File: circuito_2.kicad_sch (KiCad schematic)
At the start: 25 parts, among them U1 TL081, U2 TL081, U3 TL081

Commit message: Reorganização dos esquemáticos em pages.
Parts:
- removed C1, C10, C11, C13, C15, C2, C4, C7, C8: C, symbol Device:C
- removed C12, C14, C3, C5, C6, C9: C_Polarized_US, symbol Device:C_Polarized_US
- removed R1, R2, R3, R4, R5, R6, R7: R, symbol Device:R
- removed U1, U2, U3: TL081, symbol Amplifier_Operational:TL081
- added C22, C24, C25, C28, C29, C31, C33, C34, C36: C, symbol Device:C
- added C23, C26, C27, C30, C32, C35: C_Polarized_US, symbol Device:C_Polarized_US
- added R10, R11, R12, R13, R14, R8, R9: R, symbol Device:R
- added U10, U8, U9: TL081, symbol Amplifier_Operational:TL081
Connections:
- net +15V: now also C23.1, C24.1, C27.1, C28.1, C32.1, C33.1, U10.7 (V+), U8.7 (V+), U9.7 (V+)
- net -15V: now also C25.1, C26.2, C29.1, C30.2, C34.1, C35.2, U10.4 (V-), U8.4 (V-), U9.4 (V-)
- net Earth: now also C22.2, C23.2, C24.2, C25.2, C26.1, C27.2, C28.2, C29.2, C30.1, C32.2, C33.2, C34.2, C35.1, R8.2, U9.3 (+)
- new net: C22.1, R10.1, U8.2 (-)
- new net: C36.1, R13.2, R14.1, U10.2 (-)
- new net: C36.2, R14.2, U10.6
- new net: C31.2, R12.2, R13.1, U9.6
- new net: R8.1, R9.1, U8.3 (+)
- new net: R10.2, R11.1, R9.2, U8.6
- new net: C31.1, R11.2, R12.1, U9.2 (-)

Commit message: Footprints parcialmente adicionados.
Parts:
- C10: renamed from C25; value C -> 0.1uF/50V; footprint (none) -> Capacitor_THT:C_Disc_D3.8mm_W2.6mm_P2.50mm
- C13: renamed from C28; value C -> 0.1uF/50V; footprint (none) -> Capacitor_THT:C_Disc_D3.8mm_W2.6mm_P2.50mm
- C14: renamed from C29; value C -> 0.1uF/50V; footprint (none) -> Capacitor_THT:C_Disc_D3.8mm_W2.6mm_P2.50mm
- C16: renamed from C31; value C -> 0.1uF/50V; footprint (none) -> Capacitor_THT:C_Disc_D3.8mm_W2.6mm_P2.50mm
- C18: renamed from C33; value C -> 0.1uF/50V; footprint (none) -> Capacitor_THT:C_Disc_D3.8mm_W2.6mm_P2.50mm
- C19: renamed from C34; value C -> 0.1uF/50V; footprint (none) -> Capacitor_THT:C_Disc_D3.8mm_W2.6mm_P2.50mm
- C21: renamed from C36; value C -> 0.1uF/50V; footprint (none) -> Capacitor_THT:C_Disc_D3.8mm_W2.6mm_P2.50mm
- C7: renamed from C22; value C -> 0.1uF/50V; footprint (none) -> Capacitor_THT:C_Disc_D3.8mm_W2.6mm_P2.50mm
- C9: renamed from C24; value C -> 0.1uF/50V; footprint (none) -> Capacitor_THT:C_Disc_D3.8mm_W2.6mm_P2.50mm
- renumbered C26 to C11, C27 to C12, C30 to C15, C32 to C17, C35 to C20, C23 to C8, R8 to R1, R9 to R2, R10 to R3, R11 to R4, R12 to R5, R13 to R6, R14 to R7, U8 to U3, U9 to U4, U10 to U5
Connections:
- net Senoidal: now reaches C21.2, R7.2, U5.6
- net Triangular: now reaches C16.2, R5.2, R6.1, U4.6
- net Quadrada: now reaches R2.2, R3.2, R4.1, U3.6

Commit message: Relação de footprints finalizada.
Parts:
- C11, C12, C15, C17, C20, C8: value C_Polarized_US -> 10uF/25V; footprint (none) -> Capacitor_THT:CP_Radial_D4.0mm_P2.00mm
- R1, R2, R3, R4, R5, R6, R7: footprint (none) -> Resistor_THT:R_Axial_DIN0207_L6.3mm_D2.5mm_P2.54mm_Vertical
- U3, U4, U5: footprint (none) -> Package_DIP:DIP-8_W7.62mm_LongPads
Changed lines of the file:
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@@
 			)
 		)
-		(property "Value" "C_Polarized_US"
+		(property "Value" "10uF/25V"
 			(at 75.565 106.68 90)
 			(effects
@@
 			)
 		)
-		(property "Footprint" ""
+		(property "Footprint" "Capacitor_THT:CP_Radial_D4.0mm_P2.00mm"
 			(at 74.93 111.76 0)
 			(effects
@@
 			)
 		)
-		(property "Value" "C_Polarized_US"
+		(property "Value" "10uF/25V"
 			(at 132.715 58.42 90)
 			(effects
@@
 			)
 		)
-		(property "Footprint" ""
+		(property "Footprint" "Capacitor_THT:CP_Radial_D4.0mm_P2.00mm"
 			(at 133.35 63.5 0)
 			(effects
@@
 			)
 		)
-		(property "Footprint" ""
+		(property "Footprint" "Resistor_THT:R_Axial_DIN0207_L6.3mm_D2.5mm_P2.54mm_Vertical"
 			(at 196.85 137.668 90)
 			(effects
@@
 			)
 		)
-		(property "Value" "C_Polarized_US"
+		(property "Value" "10uF/25V"
 			(at 74.295 59.69 90)
 			(effects
@@
 			)
 		)
-		(property "Footprint" ""
+		(property "Footprint" "Capacitor_THT:CP_Radial_D4.0mm_P2.00mm"
 			(at 74.93 64.77 0)
 			(effects
@@
 			)
 		)
-		(property "Footprint" ""
+		(property "Footprint" "Resistor_THT:R_Axial_DIN0207_L6.3mm_D2.5mm_P2.54mm_Vertical"
 			(at 163.83 85.598 90)
 			(effects
@@
 			)
 		)
-		(property "Footprint" ""
+		(property "Footprint" "Package_DIP:DIP-8_W7.62mm_LongPads"
 			(at 74.93 85.09 0)
 			(effects
@@
 			)
 		)
-		(property "Footprint" ""
+		(property "Footprint" "Resistor_THT:R_Axial_DIN0207_L6.3mm_D2.5mm_P2.54mm_Vertical"
 			(at 83.82 124.968 90)
 			(effects
@@
 			)
 		)
-		(property "Footprint" ""
+		(property "Footprint" "Resistor_THT:R_Axial_DIN0207_L6.3mm_D2.5mm_P2.54mm_Vertical"
 			(at 106.68 88.138 90)
 			(effects
@@
 			)
 		)
-		(property "Footprint" ""
+		(property "Footprint" "Resistor_THT:R_Axial_DIN0207_L6.3mm_D2.5mm_P2.54mm_Vertical"
 			(at 62.23 47.498 90)
 			(effects
@@
 			)
 		)
-		(property "Footprint" ""
+		(property "Footprint" "Package_DIP:DIP-8_W7.62mm_LongPads"
 			(at 194.31 80.01 0)
 			(effects
@@
 			)
 		)
-		(property "Footprint" ""
+		(property "Footprint" "Resistor_THT:R_Axial_DIN0207_L6.3mm_D2.5mm_P2.54mm_Vertical"
 			(at 135.89 140.208 90)
 			(effects
@@
 			)
 		)
-		(property "Value" "C_Polarized_US"
+		(property "Value" "10uF/25V"
 			(at 193.675 55.88 90)
 			(effects
@@
 			)
 		)
-		(property "Footprint" ""
+		(property "Footprint" "Capacitor_THT:CP_Radial_D4.0mm_P2.00mm"
 			(at 194.31 60.96 0)
 			(effects
@@
 			)
 		)
-		(property "Footprint" ""
+		(property "Footprint" "Resistor_THT:R_Axial_DIN0207_L6.3mm_D2.5mm_P2.54mm_Vertical"
 			(at 40.132 99.06 90)
 			(effects
@@
 			)
 		)
-		(property "Footprint" ""
+		(property "Footprint" "Package_DIP:DIP-8_W7.62mm_LongPads"
 			(at 133.35 82.55 0)
 			(effects
@@
 			)
 		)
-		(property "Value" "C_Polarized_US"
+		(property "Value" "10uF/25V"
 			(at 194.945 101.6 90)
 			(effects
@@
 			)
 		)
-		(property "Footprint" ""
+		(property "Footprint" "Capacitor_THT:CP_Radial_D4.0mm_P2.00mm"
 			(at 194.31 106.68 0)
 			(effects
@@
 			)
 		)
-		(property "Value" "C_Polarized_US"
+		(property "Value" "10uF/25V"
 			(at 133.985 104.14 90)
 			(effects
@@
 			)
 		)
-		(property "Footprint" ""
+		(property "Footprint" "Capacitor_THT:CP_Radial_D4.0mm_P2.00mm"
 			(at 133.35 109.22 0)
 			(effects

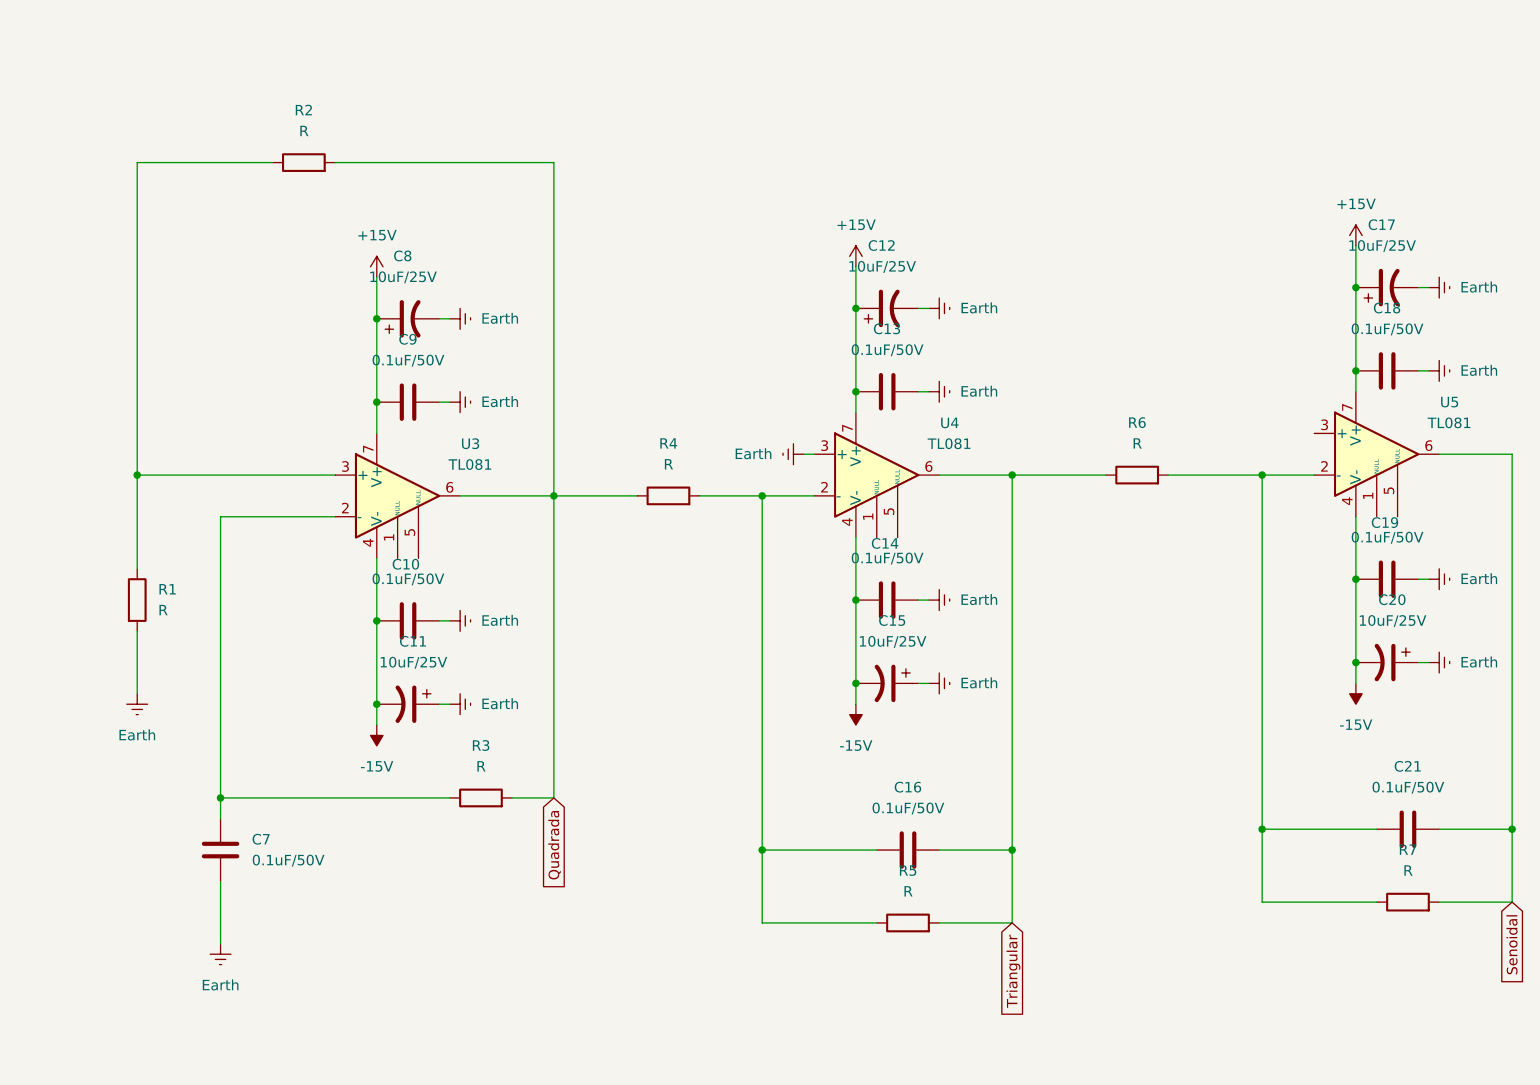
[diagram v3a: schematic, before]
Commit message: Alterações no schematic para bater com o que o professor mandoou no gropo. Pendente revisão.
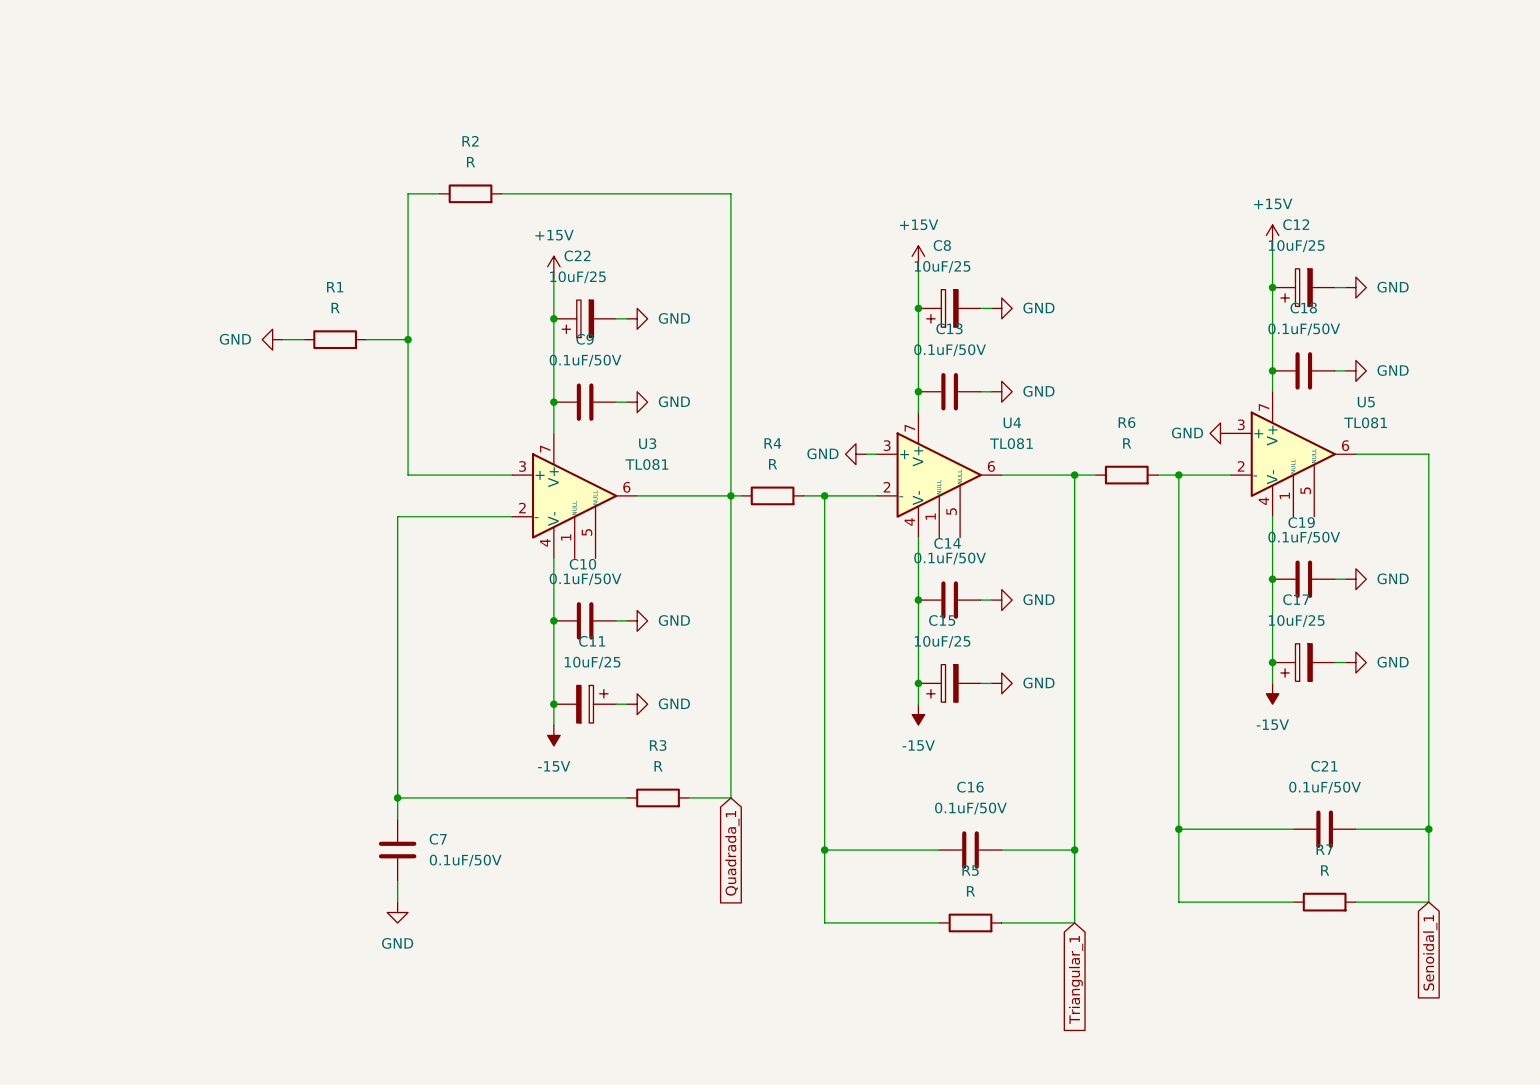
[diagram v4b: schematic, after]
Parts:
- removed C11, C12, C15, C17, C20, C8: 10uF/25V, Capacitor_THT:CP_Radial_D4.0mm_P2.00mm, symbol Device:C_Polarized_US
- added C11, C12, C15, C17, C22, C8: 10uF/25, Capacitor_THT:CP_Radial_D4.0mm_P2.00mm, symbol Device:C_Polarized
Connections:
- net +15V: now also C12.1, C22.1, C8.1
- net -15V: now also C11.2, C15.1, C17.1
- net at R2.1, U3.3 (+): now also R1.2; no longer R1.1
- net GND: now reaches U5.3 (+)
- net GND: now also C10.2, C13.2, C14.2, C18.2, C19.2, C7.2, C9.2, R1.1, U4.3 (+), C11.1, C12.2, C15.2, C17.2, C22.2, C8.2
- removed net Earth: C10.2, C13.2, C14.2, C18.2, C19.2, C7.2, C9.2, R1.2, U4.3 (+)
- net Quadrada renamed Quadrada_1
- net Senoidal renamed Senoidal_1
- net Triangular renamed Triangular_1
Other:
- moved on the sheet: C10, C13, C14, C16, C18, C19, C21, C7, C9, R1, R2, R3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

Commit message: Revisão de schematics finalizado. Posicionamentos dos componentes do circuito 1 e 2 no PCB editor.
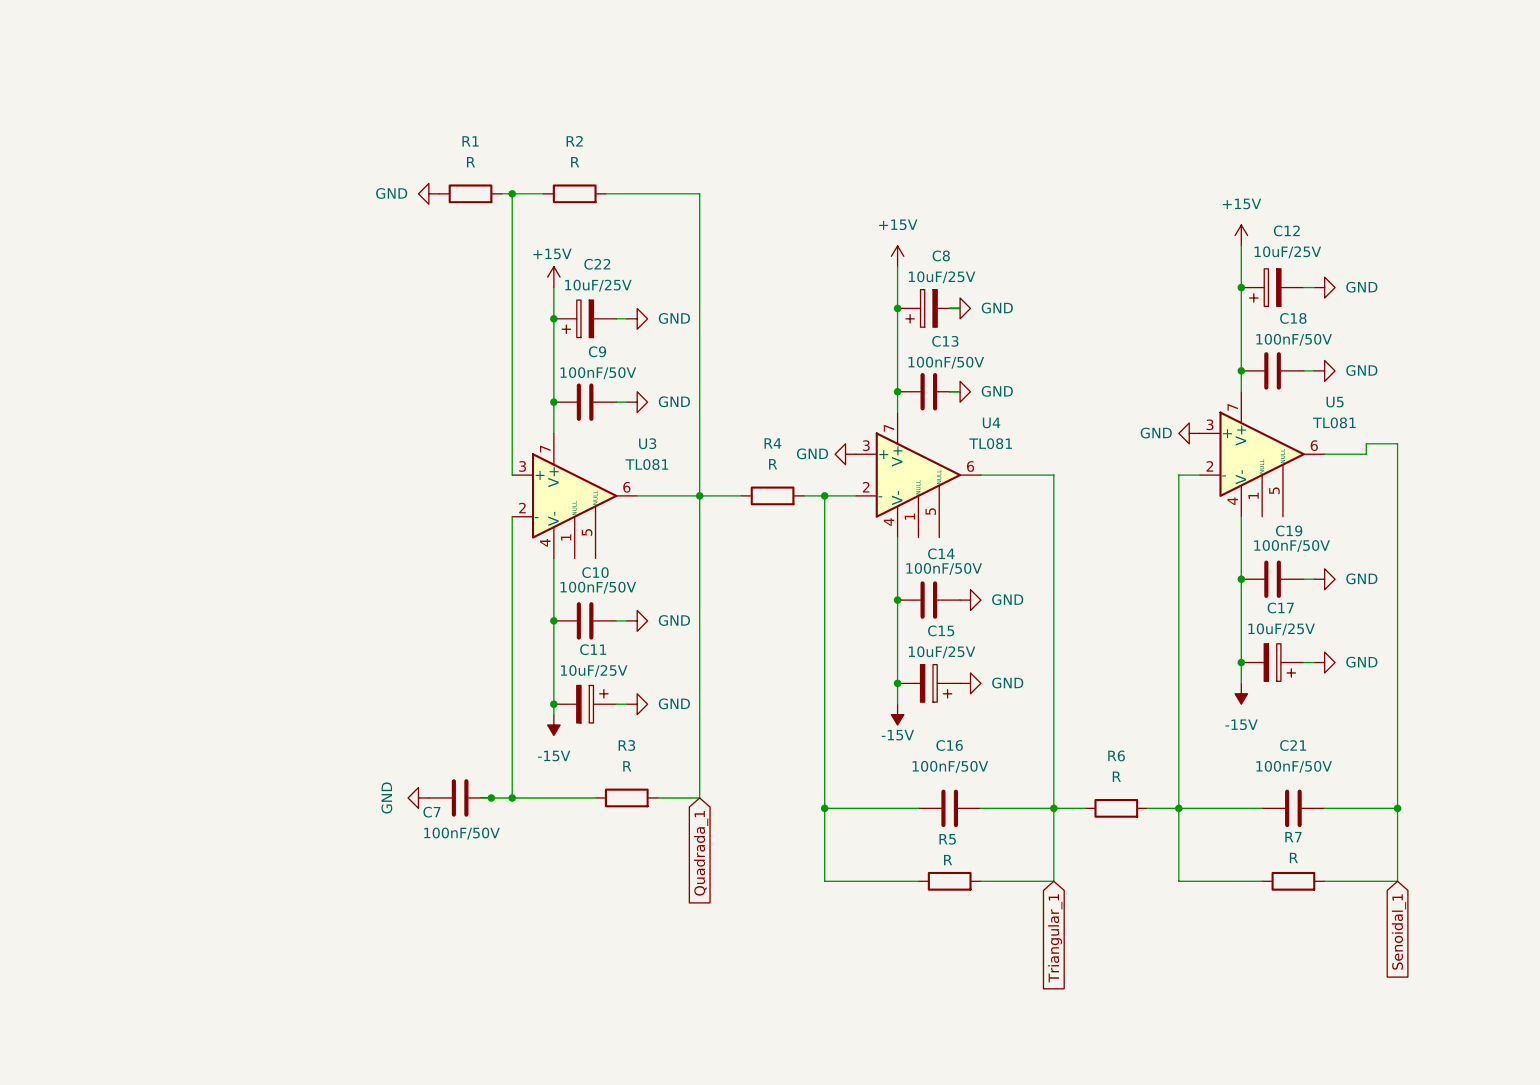
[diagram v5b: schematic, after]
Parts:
- C10, C13, C14, C16, C18, C19, C21, C7, C9: value 0.1uF/50V -> 100nF/50V; footprint Capacitor_THT:C_Disc_D3.8mm_W2.6mm_P2.50mm -> Capacitor_SMD:C_0805_2012Metric
- C11, C12, C15, C17, C22, C8: value 10uF/25 -> 10uF/25V; footprint Capacitor_THT:CP_Radial_D4.0mm_P2.00mm -> Capacitor_SMD:CP_Elec_4x5.8
- R1, R2, R3, R4, R5, R6, R7: footprint Resistor_THT:R_Axial_DIN0207_L6.3mm_D2.5mm_P2.54mm_Vertical -> Resistor_SMD:R_0805_2012Metric
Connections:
- net -15V: now also C15.2, C17.2; no longer C15.1, C17.1
- net GND: now also C15.1, C17.1; no longer C15.2, C17.2
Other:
- moved on the sheet: C12, C13, C14, C15, C16, C17, C18, C19, C21, C7, C8, R1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

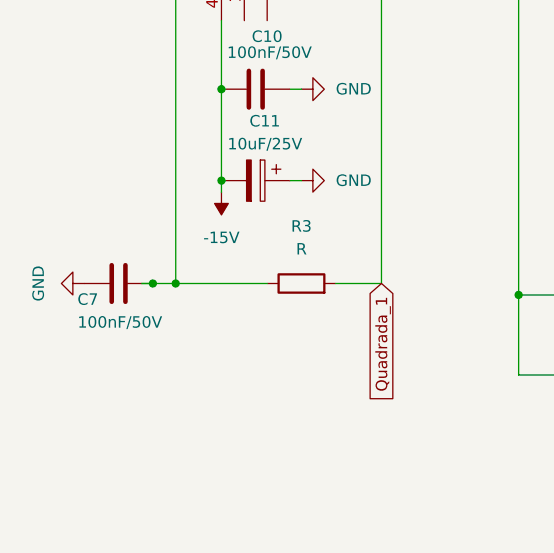
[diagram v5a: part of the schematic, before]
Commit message: Finalização de posicionamento de componentes no PCB, REVISÃO PENDENTE!!!
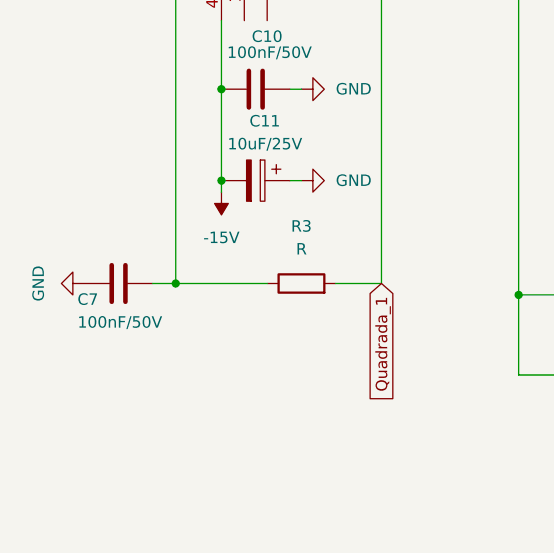
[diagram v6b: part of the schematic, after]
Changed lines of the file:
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@@
-	)
-	(junction
-		(at 85.09 123.19)
-		(diameter 0)
-		(color 0 0 0 0)
 	)
 	(junction
@@
 	(wire
 		(pts
-			(xy 83.82 123.19) (xy 85.09 123.19)
+			(xy 85.09 123.19) (xy 87.63 123.19)
 		)
 		(stroke
@@
 		)
 		(stroke
-			(width 0)
-			(type default)
-		)
-	)
-	(wire
-		(pts
-			(xy 85.09 123.19) (xy 87.63 123.19)
-		)
-		(stroke
